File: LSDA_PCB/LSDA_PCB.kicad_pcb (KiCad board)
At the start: 2 copper layers, 41.9 x 99.1 mm, 37 parts, among them Q1 BC547, Q2 BC547, U1 LM324

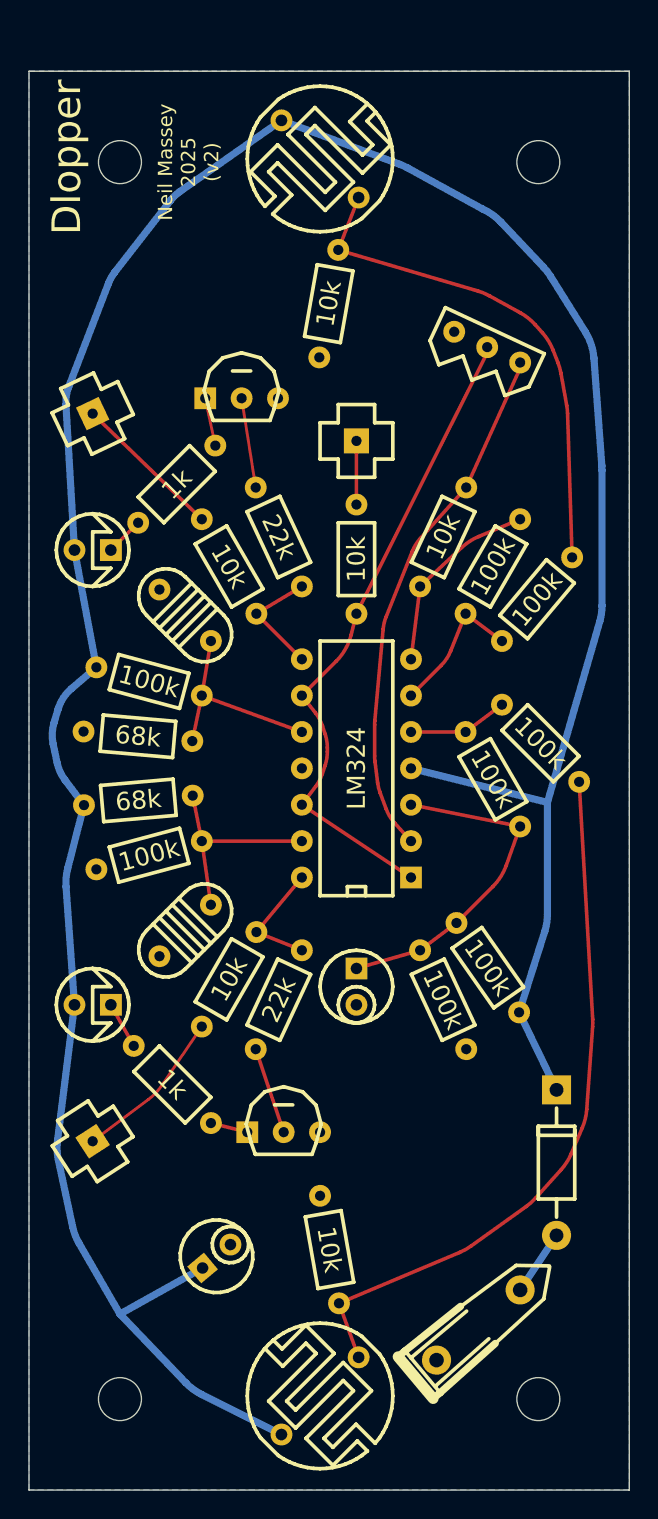
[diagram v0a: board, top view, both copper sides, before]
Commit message: Mounting holes
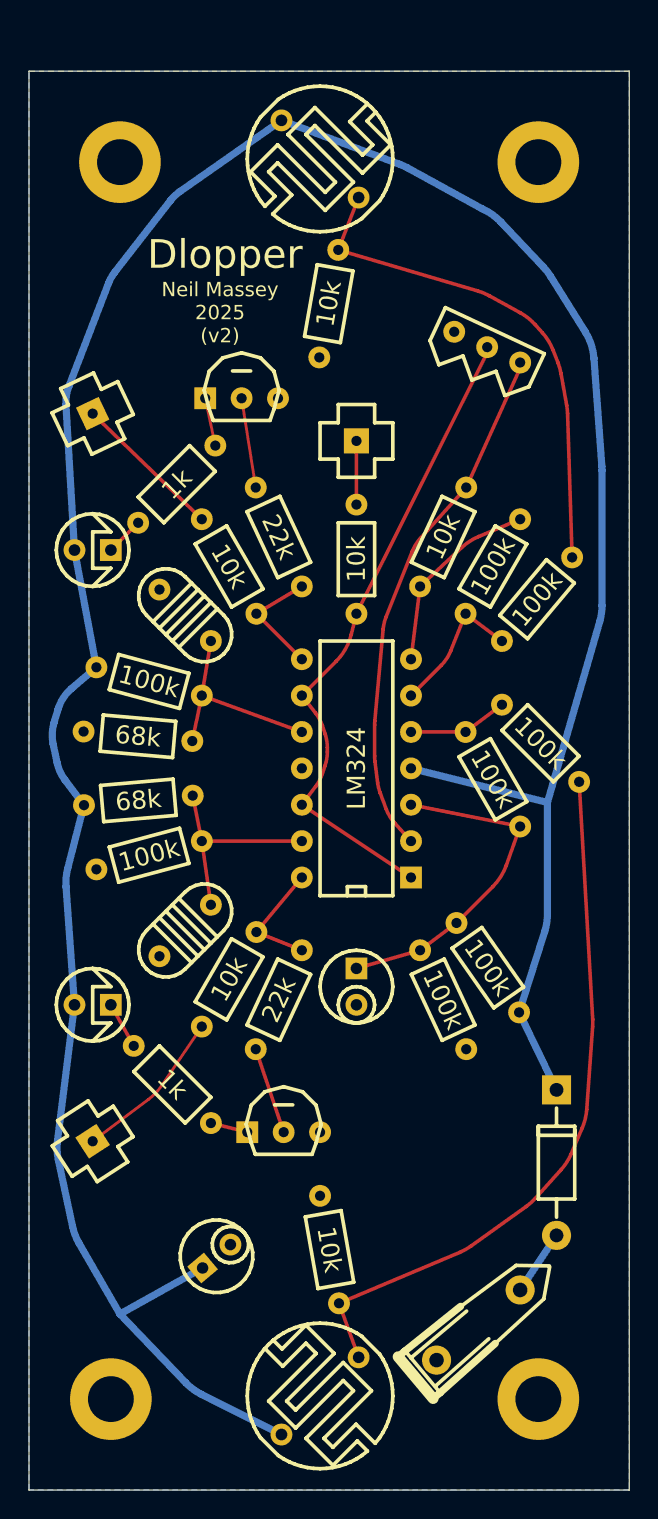
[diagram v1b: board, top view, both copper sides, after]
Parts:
- added H1: MountingHole_Pad_MP, MountingHole:MountingHole_3.2mm_M3_ISO7380_Pad, F.Cu at (50.8, 21.6)
- added H2: MountingHole_Pad_MP, MountingHole:MountingHole_3.2mm_M3_ISO7380_Pad, F.Cu at (50.8, 108.0)
- added H3: MountingHole_Pad_MP, MountingHole:MountingHole_3.2mm_M3_ISO7380_Pad, F.Cu at (21.0, 108.0)
- added H4: MountingHole_Pad_MP, MountingHole:MountingHole_3.2mm_M3_ISO7380_Pad, F.Cu at (21.6, 21.6)
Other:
- outline, holes or cut-outs redrawn
